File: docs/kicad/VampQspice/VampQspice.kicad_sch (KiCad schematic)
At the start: 19 parts, among them Q1 BC847, Q2 BC847

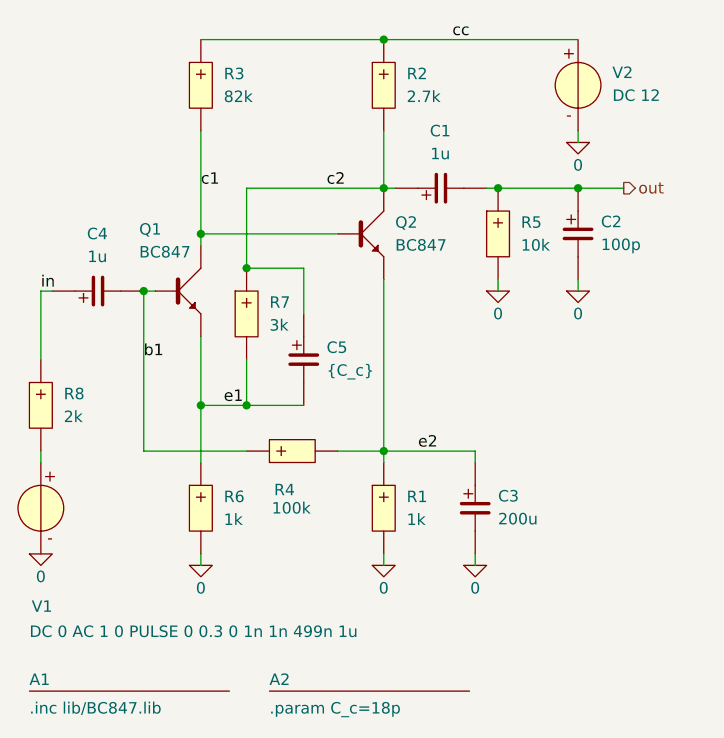
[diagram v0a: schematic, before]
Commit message: Added KiCAD NGspice schematic operating poit annotation
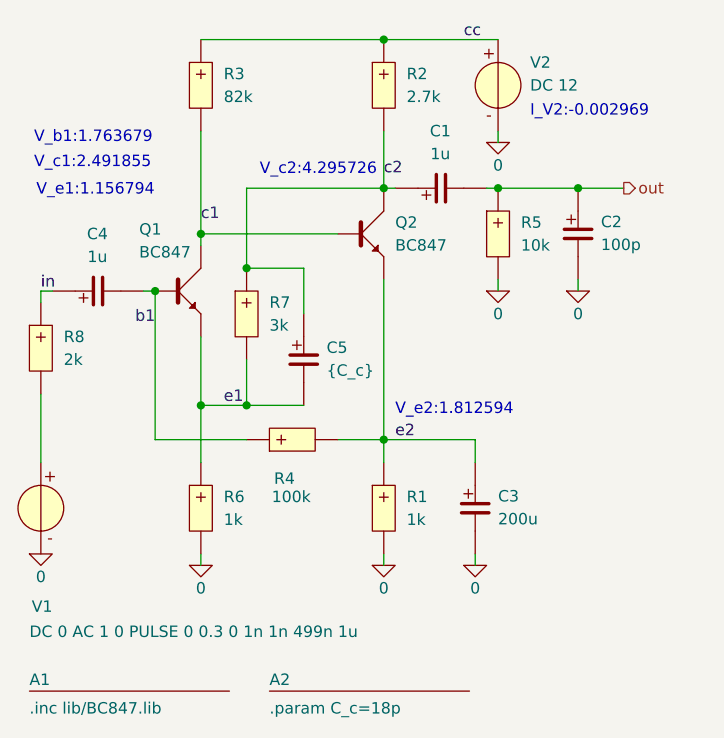
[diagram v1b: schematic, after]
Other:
- note added: "I_V2:-0.002969"
- note added: "V_b1:1.763679"
- note added: "V_c1:2.491855"
- note added: "V_c2:4.295726"
- note added: "V_e1:1.156794"
- note added: "V_e2:1.812594"
- moved on the sheet: R4, R8, V2

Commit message: Version 4.0.10 update
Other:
- note added: "I_V2: -2.97e-03"
- note added: "V_b1: 1.76e+00"
- note added: "V_c1: 2.49e+00"
- note added: "V_c2: 4.30e+00"
- note added: "V_e1: 1.16e+00"
- note added: "V_e2: 1.81e+00"
- note removed: "I_V2:-0.002969"
- note removed: "V_b1:1.763679"
- note removed: "V_c1:2.491855"
- note removed: "V_c2:4.295726"
- note removed: "V_e1:1.156794"
- note removed: "V_e2:1.812594"
